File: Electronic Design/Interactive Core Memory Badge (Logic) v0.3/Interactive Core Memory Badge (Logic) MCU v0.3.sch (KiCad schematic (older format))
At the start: 14 parts, among them U2 Teensy-LC

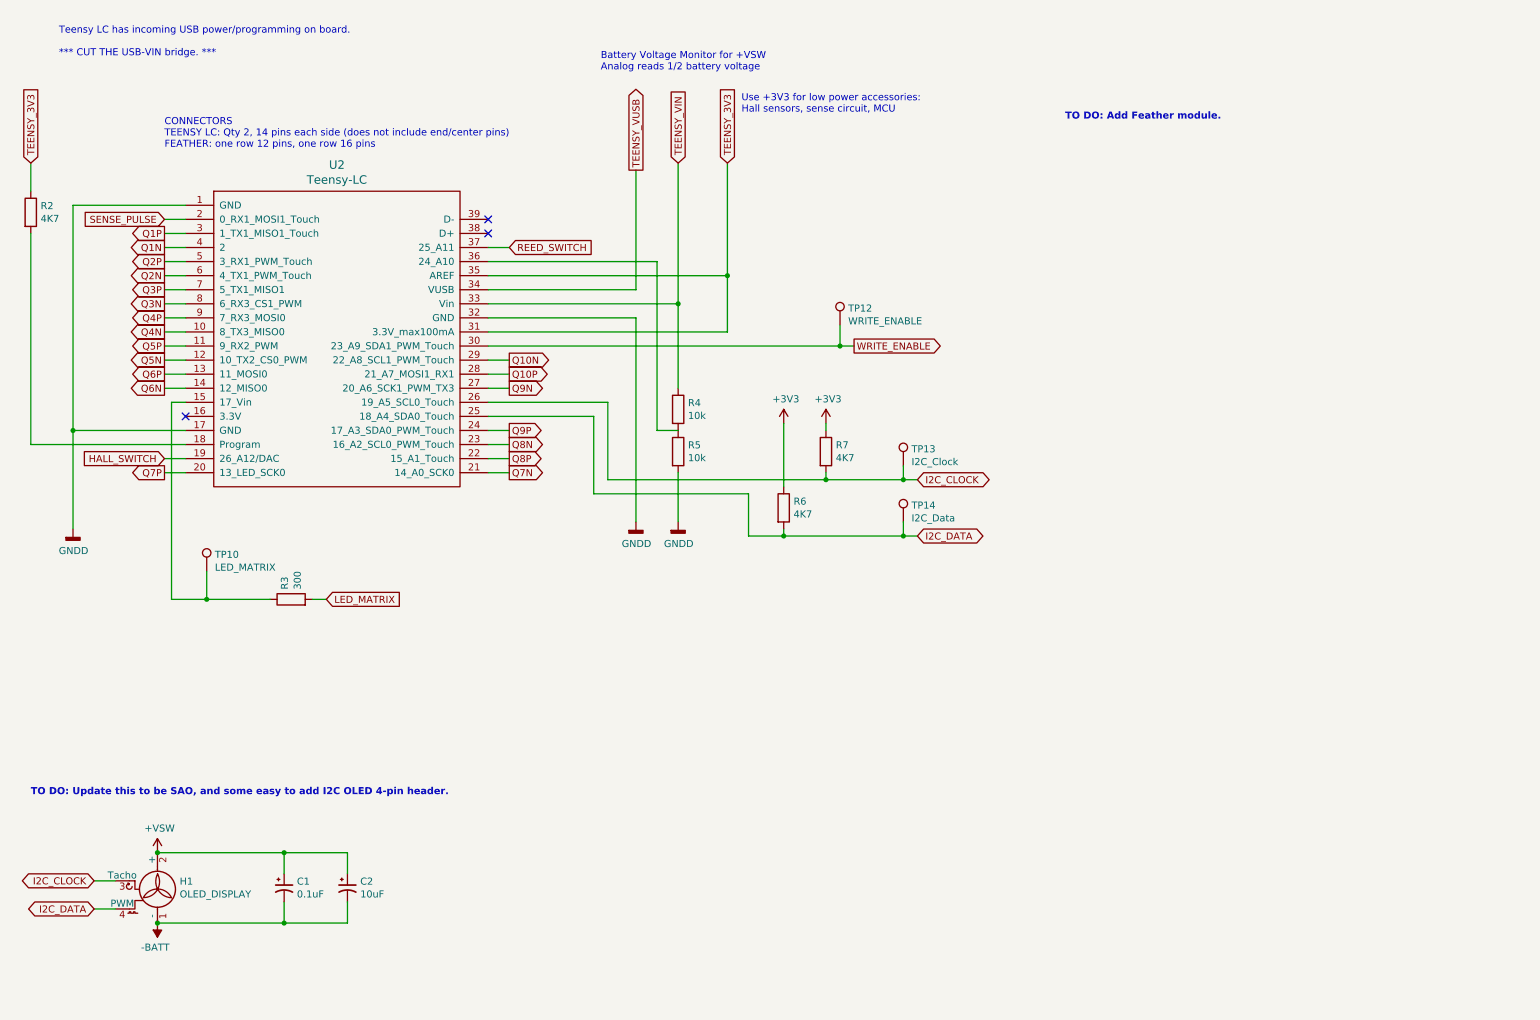
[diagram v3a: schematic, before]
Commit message: Add sense NORs and IO expansion and NOTs.
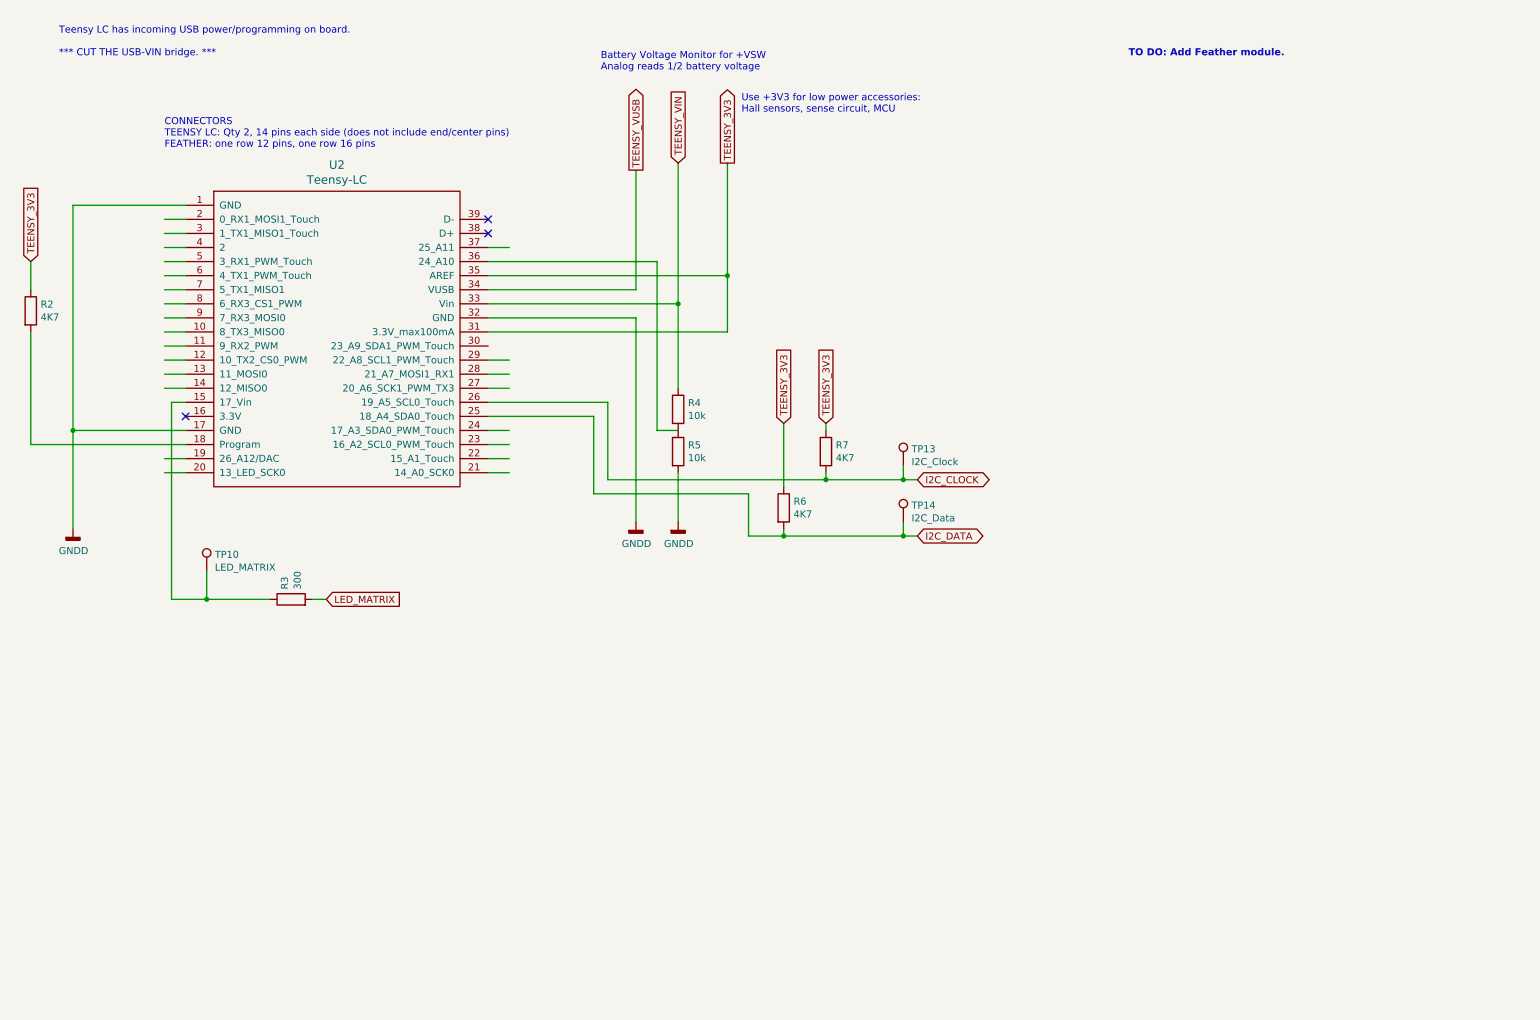
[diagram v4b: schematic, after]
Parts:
- removed C1: 0.1uF, Capacitor_SMD:C_0805_2012Metric, symbol Device:CP1_Small
- removed C2: 10uF, Capacitor_SMD:C_0805_2012Metric, symbol Device:CP1_Small
- removed H1: OLED_DISPLAY, Core_Memory_8x8_Array:OLED_Header_4PIN, symbol Motor:Fan_4pin
- removed TP12: WRITE_ENABLE, TestPoint:TestPoint_Keystone_5000-5004_Miniature, symbol Connector:TestPoint
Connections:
- net labels removed: +3V3, +VSW, -BATT, HALL_SWITCH, Q10N, Q10P, Q1N, Q1P, Q2N, Q2P, Q3N, Q3P, Q4N, Q4P, Q5N, Q5P, Q6N, Q6P, Q7N, Q7P, Q8N, Q8P, Q9N, Q9P, REED_SWITCH, SENSE_PULSE, WRITE_ENABLE
- wire segments 82 -> 69
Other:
- note removed: "TO DO: Update this to be SAO, and some easy to add I2C OLED 4-pin header."
- moved on the sheet: R2
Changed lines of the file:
@@
 $Descr A4 11693 8268
 encoding utf-8
-Sheet 3 5
+Sheet 3 6
 Title "Core 64 - MCU Logic"
 Date "2020-03-15"
@@
 	1    0    0    -1
 $EndComp
-Text GLabel 1650 2150 0    50   Output ~ 0
-Q1P
-Text GLabel 1650 2250 0    50   Output ~ 0
-Q1N
 Wire Wire Line
 	1650 2150 1800 2150
@@
 Wire Wire Line
 	4800 3350 4800 3900
-$Comp
-L power:+3V3 #PWR0123
-U 1 1 5D3544A4
-P 6350 3500
-AR Path="/5E755787/5D3544A4" Ref="#PWR0123"  Part="1"
-AR Path="/5E755AC8/5D2551FF/5D3544A4" Ref="#PWR?"  Part="1"
-F 0 "#PWR0123" H 6350 3350 50  0001 C CNN
-F 1 "+3V3" H 6365 3673 50  0000 C CNN
-F 2 "" H 6350 3500 50  0001 C CNN
-F 3 "" H 6350 3500 50  0001 C CNN
-	1    6350 3500
-	1    0    0    -1
-$EndComp
-$Comp
-L power:+3V3 #PWR0124
-U 1 1 5D3556B5
-P 6050 3500
-AR Path="/5E755787/5D3556B5" Ref="#PWR0124"  Part="1"
-AR Path="/5E755AC8/5D2551FF/5D3556B5" Ref="#PWR?"  Part="1"
-F 0 "#PWR0124" H 6050 3350 50  0001 C CNN
-F 1 "+3V3" H 6065 3673 50  0000 C CNN
-F 2 "" H 6050 3500 50  0001 C CNN
-F 3 "" H 6050 3500 50  0001 C CNN
-	1    6050 3500
-	1    0    0    -1
-$EndComp
-Text GLabel 6550 2950 2    50   Output ~ 0
-WRITE_ENABLE
-Wire Wire Line
-	3950 2950 6450 2950
-Text GLabel 1650 2050 0    50   Input ~ 0
-SENSE_PULSE
 Wire Wire Line
 	1650 2050 1800 2050
-Text GLabel 1650 2350 0    50   Output ~ 0
-Q2P
-Text GLabel 1650 2450 0    50   Output ~ 0
-Q2N
 Wire Wire Line
 	1650 2350 1800 2350
 Wire Wire Line
 	1650 2450 1800 2450
-Text GLabel 1650 2550 0    50   Output ~ 0
-Q3P
-Text GLabel 1650 2650 0    50   Output ~ 0
-Q3N
 Wire Wire Line
 	1650 2550 1800 2550
 Wire Wire Line
 	1650 2650 1800 2650
-Text GLabel 1650 2750 0    50   Output ~ 0
-Q4P
-Text GLabel 1650 2850 0    50   Output ~ 0
-Q4N
 Wire Wire Line
 	1650 2750 1800 2750
 Wire Wire Line
 	1650 2850 1800 2850
-Text GLabel 1650 2950 0    50   Output ~ 0
-Q5P
-Text GLabel 1650 3050 0    50   Output ~ 0
-Q5N
 Wire Wire Line
 	1650 2950 1800 2950
 Wire Wire Line
 	1650 3050 1800 3050
-Text GLabel 1650 3150 0    50   Output ~ 0
-Q6P
-Text GLabel 1650 3250 0    50   Output ~ 0
-Q6N
 Wire Wire Line
 	1650 3150 1800 3150
@@
 	1800 3550 1000 3550
 Connection ~ 1000 3550
-Text GLabel 1650 3850 0    50   Output ~ 0
-Q7P
 Wire Wire Line
 	1650 3850 1800 3850
@@
 Wire Wire Line
 	3950 3650 4100 3650
-Text GLabel 4100 3550 2    50   Output ~ 0
-Q9P
 Wire Wire Line
 	3950 3550 4100 3550
-Text GLabel 4100 3650 2    50   Output ~ 0
-Q8N
-Text GLabel 4100 3750 2    50   Output ~ 0
-Q8P
-Text GLabel 4100 3850 2    50   Output ~ 0
-Q7N
 Wire Wire Line
 	3950 3250 4100 3250
@@
 Wire Wire Line
 	3950 3050 4100 3050
-Text GLabel 4100 3050 2    50   Output ~ 0
-Q10N
-Text GLabel 4100 3150 2    50   Output ~ 0
-Q10P
-Text GLabel 4100 3250 2    50   Output ~ 0
-Q9N
-Text GLabel 4100 2250 2    50   Input ~ 0
-REED_SWITCH
 Wire Wire Line
 	3950 2250 4100 2250
 NoConn ~ 1800 3450
-Text GLabel 1650 3750 0    50   Input ~ 0
-HALL_SWITCH
 Wire Wire Line
 	1650 3750 1800 3750
 Text GLabel 2800 4750 2    50   Input ~ 0
 LED_MATRIX
-$Comp
-L Motor:Fan_4pin H1
-U 1 1 5D49F2EF
-P 1600 6850
-AR Path="/5E755787/5D49F2EF" Ref="H1"  Part="1"
-AR Path="/5E755AC8/5D2551FF/5D49F2EF" Ref="H?"  Part="1"
-F 0 "H1" H 1758 6946 50  0000 L CNN
-F 1 "OLED_DISPLAY" H 1758 6855 50  0000 L CNN
-F 2 "Core_Memory_8x8_Array:OLED_Header_4PIN" H 1600 6860 50  0001 C CNN
-F 3 "" H 1600 6860 50  0001 C CNN
-	1    1600 6850
-	1    0    0    -1
-$EndComp
-$Comp
-L power:-BATT #PWR0128
-U 1 1 5D49FCEF
-P 1600 7050
-AR Path="/5E755787/5D49FCEF" Ref="#PWR0128"  Part="1"
-AR Path="/5E755AC8/5D2551FF/5D49FCEF" Ref="#PWR?"  Part="1"
-F 0 "#PWR0128" H 1600 6900 50  0001 C CNN
-F 1 "-BATT" H 1615 7223 50  0000 C CNN
-F 2 "" H 1600 7050 50  0001 C CNN
-F 3 "" H 1600 7050 50  0001 C CNN
-	1    1600 7050
-	-1   0    0    1
-$EndComp
-$Comp
-L power:+VSW #PWR0129
-U 1 1 5D4A026C
-P 1600 6550
-AR Path="/5E755787/5D4A026C" Ref="#PWR0129"  Part="1"
-AR Path="/5E755AC8/5D2551FF/5D4A026C" Ref="#PWR?"  Part="1"
-F 0 "#PWR0129" H 1600 6400 50  0001 C CNN
-F 1 "+VSW" H 1615 6723 50  0000 C CNN
-F 2 "" H 1600 6550 50  0001 C CNN
-F 3 "" H 1600 6550 50  0001 C CNN
-	1    1600 6550
-	1    0    0    -1
-$EndComp
-Text GLabel 1150 6750 0    50   BiDi ~ 0
-I2C_CLOCK
-Text GLabel 1150 6950 0    50   BiDi ~ 0
-I2C_DATA
 $Comp
 L Connector:TestPoint TP13
@@
 $EndComp
 $Comp
-L Connector:TestPoint TP12
-U 1 1 5D4DAE01
-P 6450 2800
-AR Path="/5E755787/5D4DAE01" Ref="TP12"  Part="1"
-AR Path="/5E755AC8/5D2551FF/5D4DAE01" Ref="TP?"  Part="1"
-F 0 "TP12" H 6508 2918 50  0000 L CNN
-F 1 "WRITE_ENABLE" H 6508 2827 50  0000 L CNN
-F 2 "TestPoint:TestPoint_Keystone_5000-5004_Miniature" H 6650 2800 50  0001 C CNN
-F 3 "~" H 6650 2800 50  0001 C CNN
-	1    6450 2800
-	1    0    0    -1
-$EndComp
-Wire Wire Line
-	6450 2800 6450 2950
-Connection ~ 6450 2950
-Wire Wire Line
-	6450 2950 6550 2950
-$Comp
 L Device:R R2
 U 1 1 5D4CBADA
-P 700 2000
+P 700 2700
 AR Path="/5E755787/5D4CBADA" Ref="R2"  Part="1"
 AR Path="/5E755AC8/5D2551FF/5D4CBADA" Ref="R?"  Part="1"
-F 0 "R2" H 770 2046 50  0000 L CNN
-F 1 "4K7" H 770 1955 50  0000 L CNN
-F 2 "Resistor_SMD:R_0805_2012Metric" V 630 2000 50  0001 C CNN
-F 3 "~" H 700 2000 50  0001 C CNN
-	1    700  2000
-	1    0    0    -1
-$EndComp
-Wire Wire Line
-	700  2150 700  3650
+F 0 "R2" H 770 2746 50  0000 L CNN
+F 1 "4K7" H 770 2655 50  0000 L CNN
+F 2 "Resistor_SMD:R_0805_2012Metric" V 630 2700 50  0001 C CNN
+F 3 "~" H 700 2700 50  0001 C CNN
+	1    700  2700
+	1    0    0    -1
+$EndComp
+Wire Wire Line
+	700  2850 700  3650
 Wire Wire Line
 	700  3650 1800 3650
 Wire Wire Line
 	4800 3900 6350 3900
-Wire Wire Line
-	1150 6750 1300 6750
-Wire Wire Line
-	1150 6950 1300 6950
-$Comp
-L Device:CP1_Small C2
-U 1 1 5E7402CF
-P 2950 6800
-AR Path="/5E755787/5E7402CF" Ref="C2"  Part="1"
-AR Path="/5E755AC8/5D2551FF/5E7402CF" Ref="C?"  Part="1"
-F 0 "C2" H 3041 6846 50  0000 L CNN
-F 1 "10uF" H 3041 6755 50  0000 L CNN
-F 2 "Capacitor_SMD:C_0805_2012Metric" H 2950 6800 50  0001 C CNN
-F 3 "~" H 2950 6800 50  0001 C CNN
-	1    2950 6800
-	1    0    0    -1
-$EndComp
-$Comp
-L Device:CP1_Small C1
-U 1 1 5E741B68
-P 2500 6800
-AR Path="/5E755787/5E741B68" Ref="C1"  Part="1"
-AR Path="/5E755AC8/5D2551FF/5E741B68" Ref="C?"  Part="1"
-F 0 "C1" H 2591 6846 50  0000 L CNN
-F 1 "0.1uF" H 2591 6755 50  0000 L CNN
-F 2 "Capacitor_SMD:C_0805_2012Metric" H 2500 6800 50  0001 C CNN
-F 3 "~" H 2500 6800 50  0001 C CNN
-	1    2500 6800
-	1    0    0    -1
-$EndComp
-Wire Wire Line
-	1600 6550 2500 6550
-Wire Wire Line
-	2950 6550 2950 6700
-Connection ~ 1600 6550
-Wire Wire Line
-	2950 6900 2950 7050
-Wire Wire Line
-	2950 7050 2500 7050
-Connection ~ 1600 7050
-Wire Wire Line
-	2500 6700 2500 6550
-Connection ~ 2500 6550
-Wire Wire Line
-	2500 6550 2950 6550
-Wire Wire Line
-	2500 6900 2500 7050
-Connection ~ 2500 7050
-Wire Wire Line
-	2500 7050 1600 7050
 $Comp
 L Device:R R3
@@
 	1000 3550 1000 4250
 $Comp
-L power:GNDD #PWR?
+L power:GNDD #PWR0120
 U 1 1 5E79D787
 P 5000 4200
-AR Path="/5E755787/5E79D787" Ref="#PWR?"  Part="1"
+AR Path="/5E755787/5E79D787" Ref="#PWR0120"  Part="1"
 AR Path="/5E755AC8/5D2551FF/5E79D787" Ref="#PWR?"  Part="1"
-F 0 "#PWR?" H 5000 3950 50  0001 C CNN
+F 0 "#PWR0120" H 5000 3950 50  0001 C CNN
 F 1 "GNDD" H 5004 4045 50  0000 C CNN
 F 2 "" H 5000 4200 50  0001 C CNN
@@
 $EndComp
 $Comp
-L power:GNDD #PWR?
+L power:GNDD #PWR0121
 U 1 1 5E7A2329
 P 5300 4200
-AR Path="/5E755787/5E7A2329" Ref="#PWR?"  Part="1"
+AR Path="/5E755787/5E7A2329" Ref="#PWR0121"  Part="1"
 AR Path="/5E755AC8/5D2551FF/5E7A2329" Ref="#PWR?"  Part="1"
-F 0 "#PWR?" H 5300 3950 50  0001 C CNN
+F 0 "#PWR0121" H 5300 3950 50  0001 C CNN
 F 1 "GNDD" H 5304 4045 50  0000 C CNN
 F 2 "" H 5300 4200 50  0001 C CNN
@@
 $EndComp
 Connection ~ 5650 2450
-Text GLabel 5650 1650 1    50   Input ~ 0
+Text GLabel 5650 1650 1    50   Output ~ 0
 TEENSY_3V3
 Wire Wire Line
 	5650 1650 5650 2450
-Text GLabel 700  1650 1    50   Input ~ 0
+Text GLabel 700  2350 1    50   Input ~ 0
 TEENSY_3V3
 Wire Wire Line
-	700  1850 700  1650
-Text Notes 700  6150 0    50   ~ 10
-TO DO: Update this to be SAO, and some easy to add I2C OLED 4-pin header.
-Text Notes 8050 1350 0    50   ~ 10
+	700  2550 700  2350
+Text Notes 8500 900  0    50   ~ 10
 TO DO: Add Feather module.
 Text GLabel 5300 1650 1    50   Input ~ 0
 TEENSY_VIN
+Text GLabel 6050 3500 1    50   Input ~ 0
+TEENSY_3V3
+Text GLabel 6350 3500 1    50   Input ~ 0
+TEENSY_3V3
 $EndSCHEMATC

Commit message: Create PDF schematics
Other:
- note added: "TO DO: Board ID setting with analog levels for two analog pins?"
- note added: "TO DO: Magnetic or NFC connection."
- note added: "TO DO: SD Card access?"
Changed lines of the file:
@@
 Text GLabel 6350 3500 1    50   Input ~ 0
 TEENSY_3V3
+Text Notes 2250 4200 0    50   ~ 10
+TO DO: Board ID setting with analog levels for two analog pins?
+Text Notes 4200 3200 0    50   ~ 10
+TO DO: SD Card access?
+Text Notes 4200 4950 0    50   ~ 10
+TO DO: Magnetic or NFC connection.
 $EndSCHEMATC
